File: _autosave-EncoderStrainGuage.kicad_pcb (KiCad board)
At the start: 2 copper layers, 116.8 x 116.8 mm, 34 parts, among them J1 Conn_01x05, J2 MM8130-2600RA2, J3 MM8130-2600RA2, Q1 NX3020NAK,215, U1 PIC16LF88-I_SO, U2 OPAMP, U3 CC2500RGP, U4 nRF51x22-QFxx, Y1 Crystal 26-27 MHZ

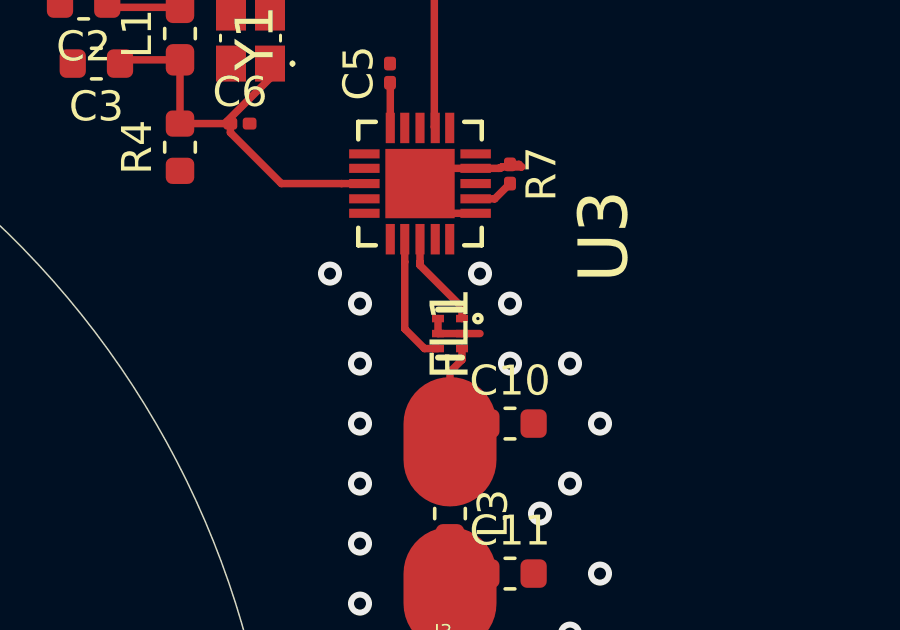
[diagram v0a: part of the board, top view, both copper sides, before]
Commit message: finished the ant module of the schematic
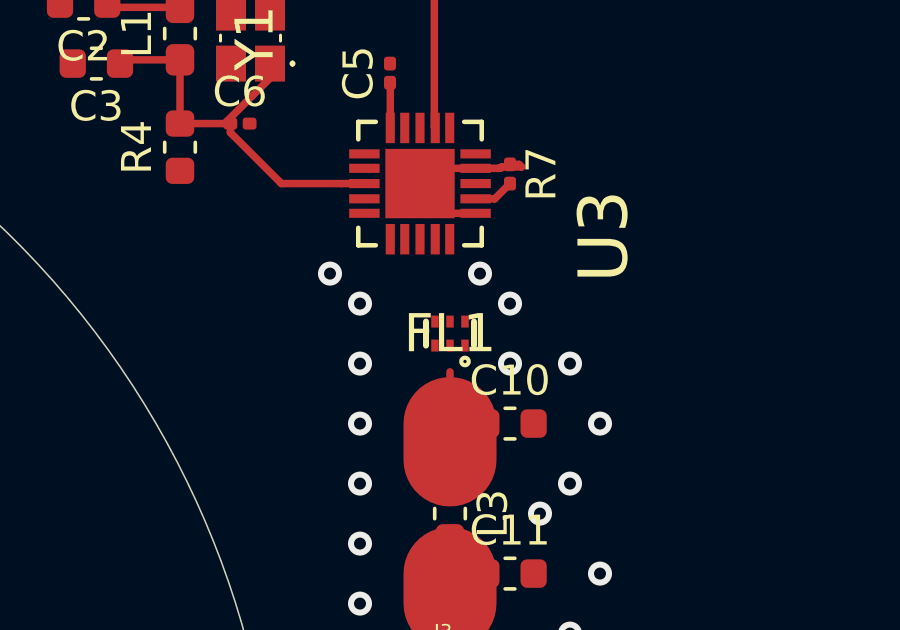
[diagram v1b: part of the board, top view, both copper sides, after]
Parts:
- turned FL1 to 0 degrees
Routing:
- net Net-(FL1-Pad4): track 4.37 -> 0.00 mm
- net Net-(FL1-Pad1): track 3.23 -> 0.00 mm
- net GND: track 8.20 -> 6.30 mm
- net Net-(C10-Pad1): track 6.51 -> 5.56 mm
